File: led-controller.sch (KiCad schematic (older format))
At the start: 7 parts, among them P1 CONN_02X20, P2 CONN_01X04, P3 CONN_01X02, Q1 IRF540N, U1 PCA9685-TSSOP

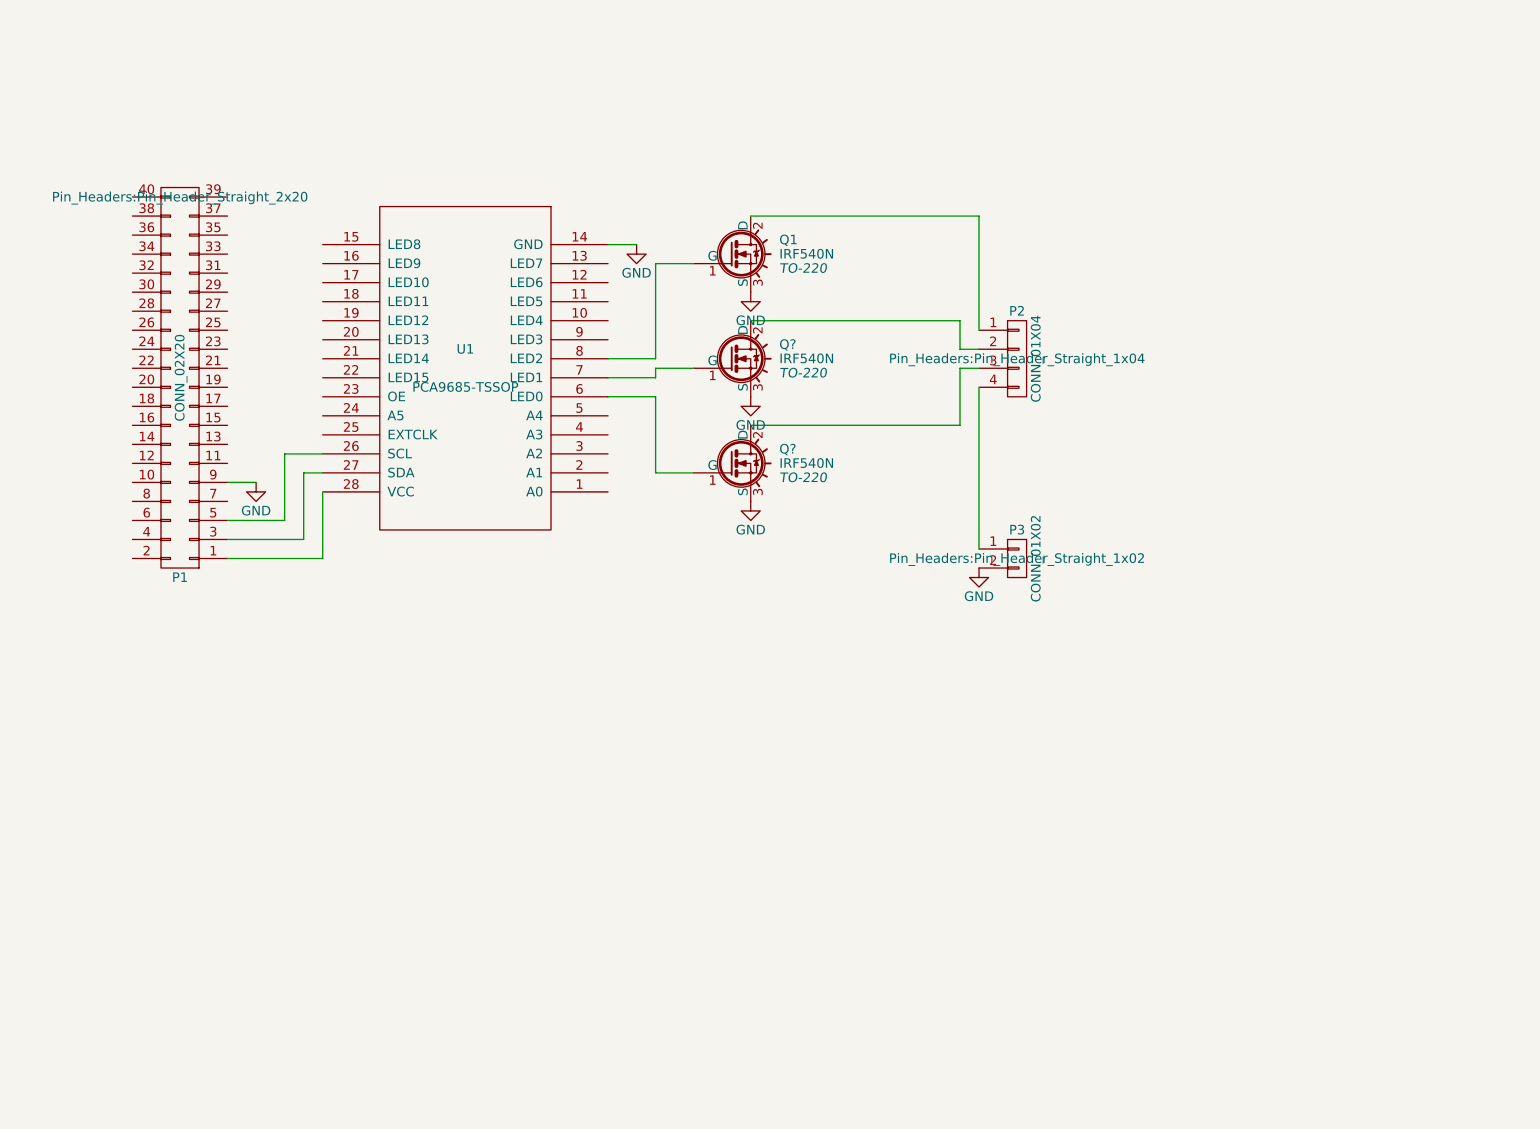
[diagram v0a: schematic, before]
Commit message: added to schema more transistors and dc dc converter
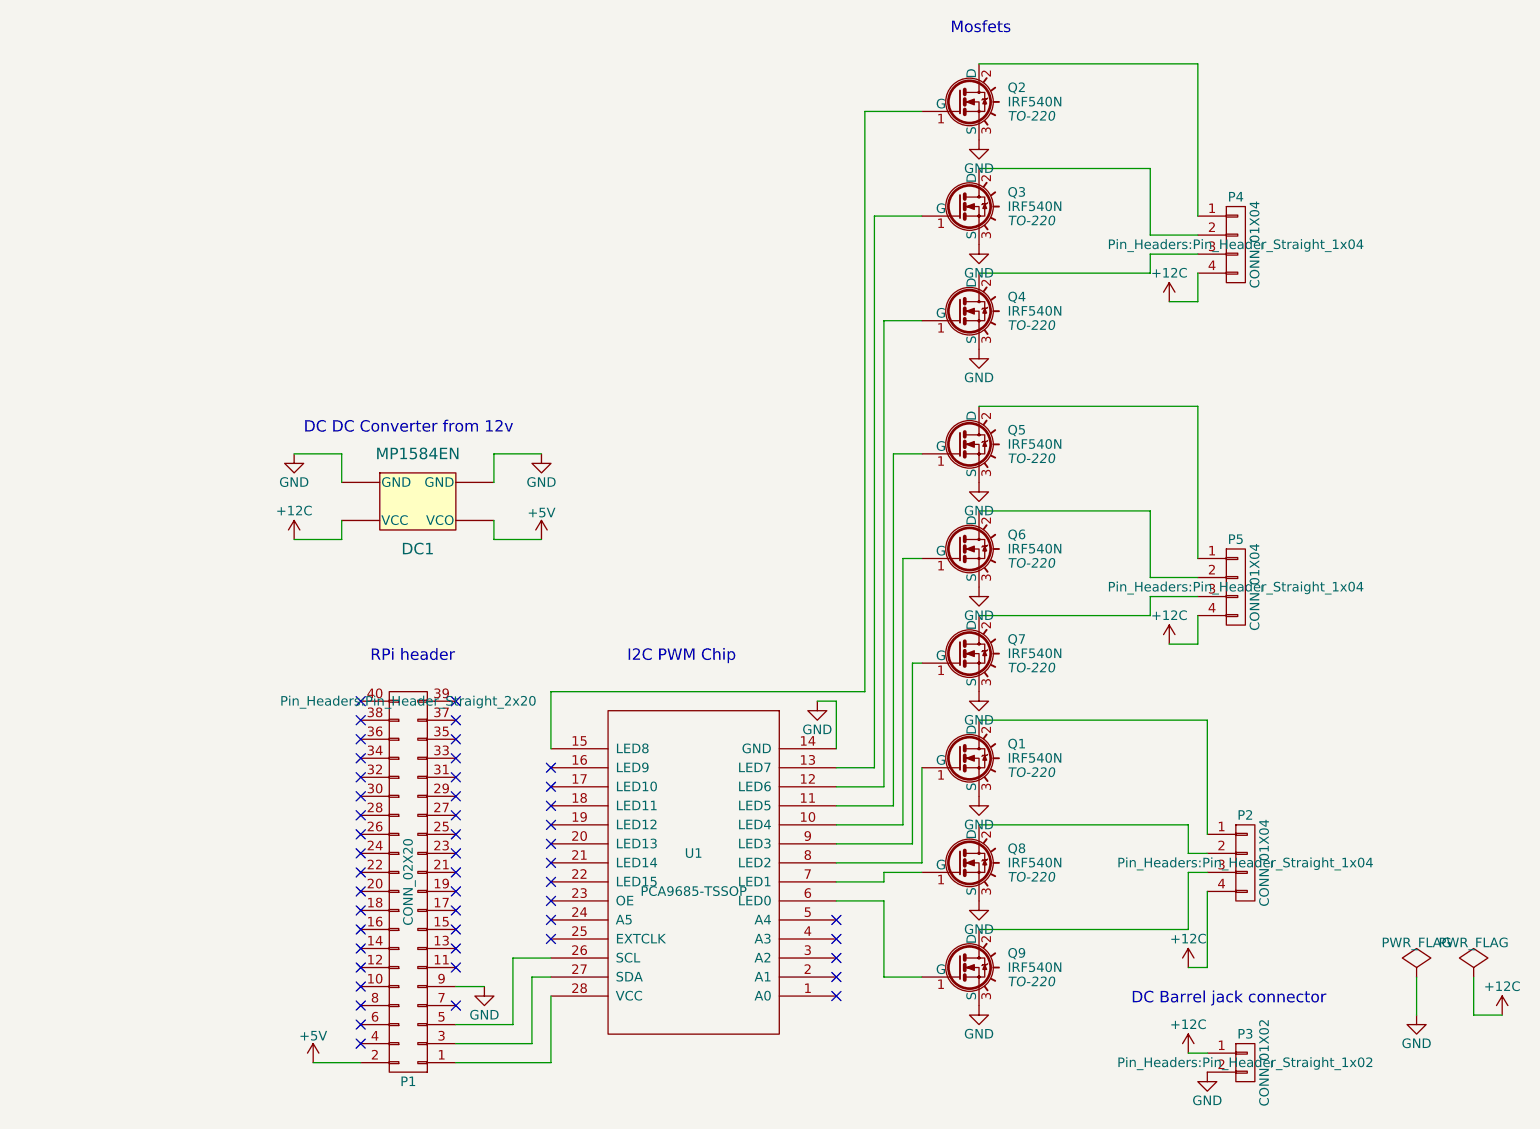
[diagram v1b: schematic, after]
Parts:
- added DC1: MP1584EN, symbol MP1584EN
- added P4, P5: CONN_01X04, Pin_Headers:Pin_Header_Straight_1x04, symbol CONN_01X04
- added Q2, Q3, Q4, Q5, Q6, Q7: IRF540N, TO-220, symbol IRF540N
- gave numbers to parts that had none: 2
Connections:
- net GND: now also DC1.~ (VCO), Q2.3 (S), Q3.3 (S), Q4.3 (S), Q5.3 (S), Q6.3 (S), Q7.3 (S)
- net at U1.10 (LED4): now also Q6.1 (G)
- net at U1.11 (LED5): now also Q5.1 (G)
- net at U1.12 (LED6): now also Q4.1 (G)
- net at U1.13 (LED7): now also Q3.1 (G)
- net at U1.15 (LED8): now also Q2.1 (G)
- net at U1.9 (LED3): now also Q7.1 (G)
- net +12C: now reaches P2.4 (P4), P3.1 (P1)
- net +12C: now also DC1.~ (VCO), P4.4 (P4), P5.4 (P4)
- net +5V: now reaches P1.2 (P2)
- net +5V: now also DC1.~ (VCO)
- new net: P5.1 (P1), Q5.2 (D)
- new net: P5.2 (P2), Q6.2 (D)
- new net: P5.3 (P3), Q7.2 (D)
- new net: P4.1 (P1), Q2.2 (D)
- new net: P4.2 (P2), Q3.2 (D)
- new net: P4.3 (P3), Q4.2 (D)
- no-connect marks 0 -> 50
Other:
- note added: "DC Barrel jack connector"
- note added: "DC DC Converter from 12v"
- note added: "I2C PWM Chip"
- note added: "Mosfets"
- note added: "RPi header"
- moved on the sheet: P1, P2, P3, Q1, Q8, Q9, U1
